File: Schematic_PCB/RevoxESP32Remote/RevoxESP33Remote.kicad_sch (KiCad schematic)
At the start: 29 parts, among them J1 SerialLink, J2 Conn_01x04, J3 Conn_01x10, J4 Conn_01x05, J5 Conn_01x04, J6 Conn_01x03, J7 Conn_01x03, Q1 BC550, Q2 2N2222, Q3 BC550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

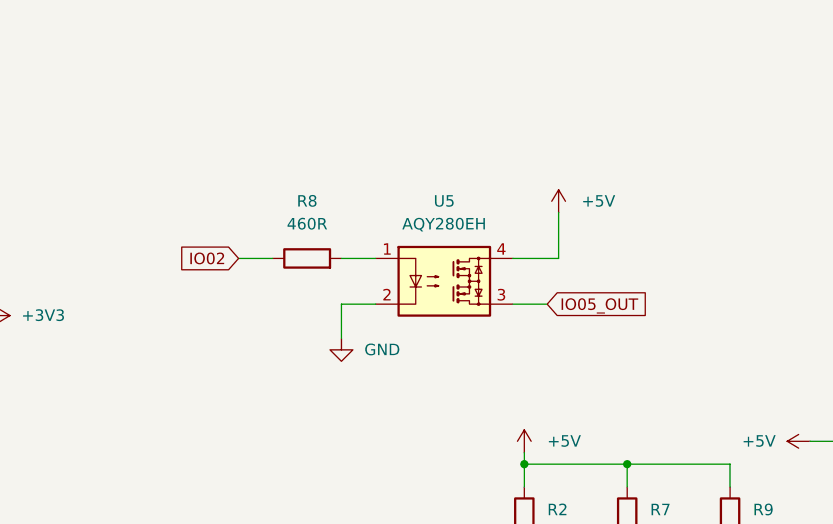
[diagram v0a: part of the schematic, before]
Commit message: IR Recive geändert, Taste gedrückt und repeat.
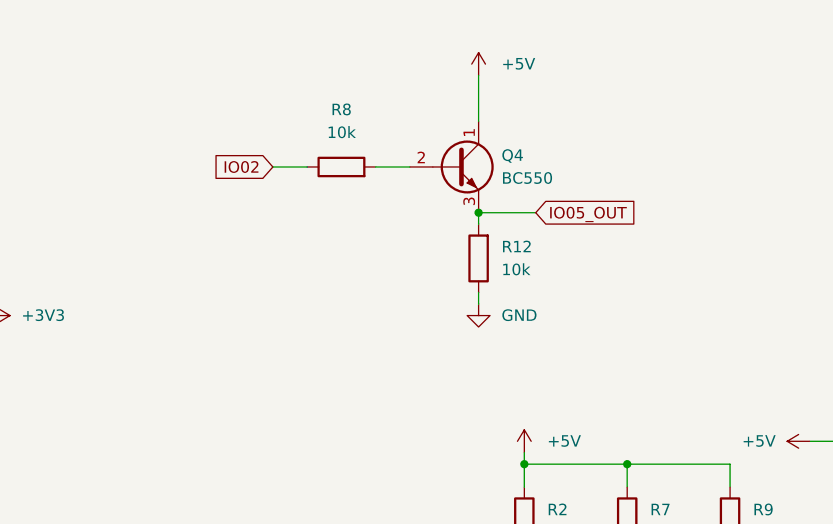
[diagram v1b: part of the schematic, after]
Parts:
- removed U5: AQY280EH, Package_DIP:DIP-4_W7.62mm, symbol Relay_SolidState:AQY280EH
- added Q4: BC550, Package_TO_SOT_THT:TO-92_Inline, symbol Transistor_BJT:BC550
- added R12: 10k, Resistor_THT:R_Axial_DIN0309_L9.0mm_D3.2mm_P12.70mm_Horizontal, symbol Device:R
- R8: value 460R -> 10k
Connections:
- net +5V: now also Q4.1 (C)
- net GND: now also R12.1
- net IO05_OUT: now also Q4.3 (E), R12.2
- net at R8.2: now also Q4.2 (B)
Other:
- moved on the sheet: R8

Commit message: IR Codes für Tape1, Tape2, Amplifier, B203, Phono und CD PLayer ergänzt.
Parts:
- C1: footprint (none) -> Capacitor_THT:CP_Radial_D8.0mm_P5.00mm
- R1, R11: footprint (none) -> Resistor_THT:R_Axial_DIN0309_L9.0mm_D3.2mm_P12.70mm_Horizontal
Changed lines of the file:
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@@
 			)
 		)
-		(property "Footprint" ""
+		(property "Footprint" "Resistor_THT:R_Axial_DIN0309_L9.0mm_D3.2mm_P12.70mm_Horizontal"
 			(at 144.272 92.71 90)
 			(hide yes)
@@
 			)
 		)
-		(property "Footprint" ""
+		(property "Footprint" "Resistor_THT:R_Axial_DIN0309_L9.0mm_D3.2mm_P12.70mm_Horizontal"
 			(at 167.132 92.71 90)
 			(hide yes)
@@
 			)
 		)
-		(property "Footprint" ""
+		(property "Footprint" "Capacitor_THT:CP_Radial_D8.0mm_P5.00mm"
 			(at 246.0752 80.01 0)
 			(hide yes)

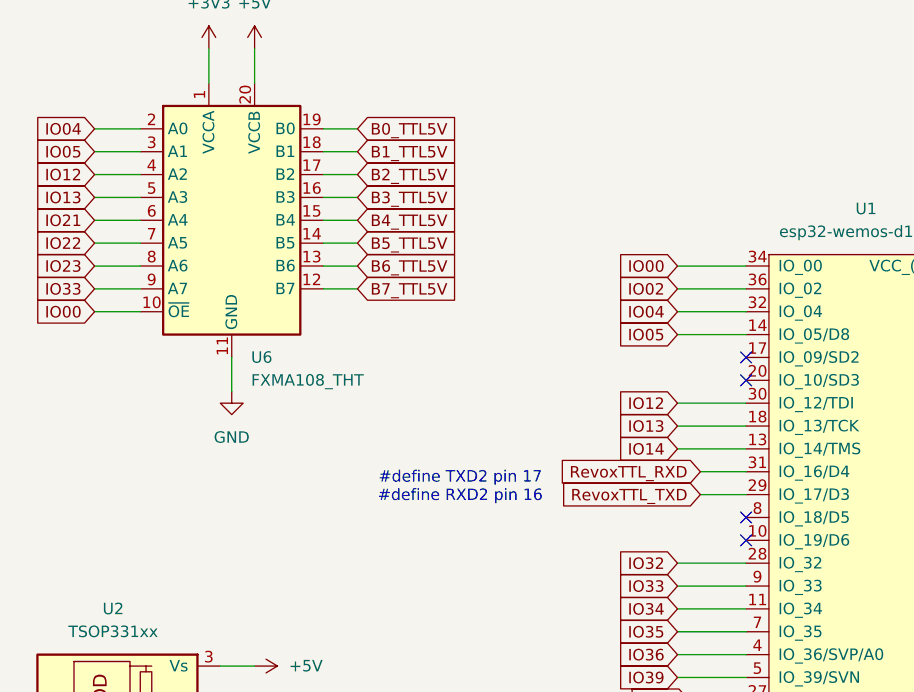
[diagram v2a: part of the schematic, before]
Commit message: Bugfix wrong RXD/TXD pins.
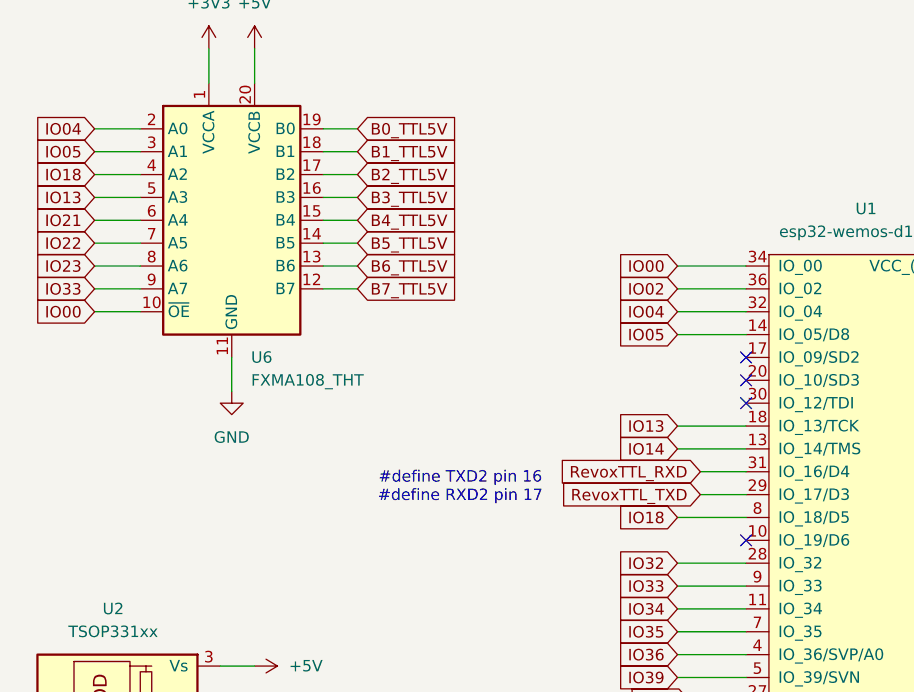
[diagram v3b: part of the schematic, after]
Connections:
- net IO18: now reaches U1.8 (IO_18/D5)
- net IO18: now also U6.4 (A2)
- net IO12: no longer names the net of U1.30 (IO_12/TDI)
- net IO12: no longer U6.4 (A2)
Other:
- note added: "#define TXD2 pin 16 #define RXD2 pin 17"
- note removed: "#define TXD2 pin 17 #define RXD2 pin 16"
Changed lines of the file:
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@@
 	(generator_version "10.0")
 	(paper "A4")
-	(text "#define TXD2 pin 17\n#define RXD2 pin 16"
+	(text "#define TXD2 pin 16\n#define RXD2 pin 17"
 		(exclude_from_sim no)
 		(at 69.85 76.708 0)
@@
 	)
 	(no_connect
-		(at 101.6 80.01)
+		(at 101.6 67.31)
 	)
 	(no_connect
@@
 	(wire
 		(pts
-			(xy 93.98 67.31) (xy 101.6 67.31)
-		)
-		(stroke
-			(width 0)
-			(type default)
-		)
-	)
-	(wire
-		(pts
 			(xy 203.2 93.98) (xy 214.63 93.98)
 		)
@@
 	(wire
 		(pts
+			(xy 93.98 80.01) (xy 101.6 80.01)
+		)
+		(stroke
+			(width 0)
+			(type default)
+		)
+	)
+	(wire
+		(pts
 			(xy 182.88 85.09) (xy 182.88 87.63)
 		)
@@
 		)
 	)
-	(global_label "IO12"
+	(global_label "IO18"
 		(shape input)
 		(at 29.21 41.91 180)
@@
 		)
 	)
-	(global_label "IO12"
-		(shape input)
-		(at 93.98 67.31 180)
-		(fields_autoplaced yes)
-		(effects
-			(font
-				(size 1.27 1.27)
-			)
-			(justify right)
-		)
-		(property "Intersheetrefs" "${INTERSHEET_REFS}"
-			(at 86.6405 67.31 0)
-			(hide yes)
-			(show_name no)
+	(global_label "IO18"
+		(shape input)
+		(at 93.98 80.01 180)
+		(fields_autoplaced yes)
+		(effects
+			(font
+				(size 1.27 1.27)
+			)
+			(justify right)
+		)
+		(property "Intersheetrefs" "${INTERSHEET_REFS}"
+			(at 86.6405 80.01 0)
+			(hide yes)
+			(show_name no)
